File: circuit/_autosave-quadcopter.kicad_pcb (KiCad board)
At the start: 4 copper layers, 37.7 x 37.7 mm, 117 parts, among them J1 Conn_01x01_Female, J10 Conn_01x01_Female, J12 Conn_01x01_Female, J13 Conn_01x01_Female, J15 Conn_01x01_Female, J16 Conn_01x01_Female, J17 Conn_01x01_Female, J18 USB_C_Receptacle_USB2.0, J19 Conn_01x08_Male, J2 Conn_01x01_Female, J21 Conn_01x01_Female, J22 Conn_01x01_Female, J23 Conn_01x01_Female, J24 Conn_01x01_Female, J25 Conn_01x01_Female, J26 Conn_01x01_Female, J28 Conn_01x01_Female, J29 Conn_01x01_Female, J30 Conn_01x01_Female, J31 Conn_01x01_Female, J32 Conn_01x01_Female, J33 Conn_01x01_Female, J34 Conn_01x01_Female, J36 Conn_01x01_Female, J37 Conn_01x01_Female, J38 Conn_01x01_Female, J39 Conn_01x01_Female, J40 Conn_01x01_Female, J41 Conn_01x01_Female, J42 Conn_01x01_Female, J43 Conn_01x01_Female, J44 Conn_01x01_Female, J45 Conn_01x01_Female, J46 Conn_01x01_Female, J47 Conn_01x01_Female, J48 Conn_01x01_Female, J49 Conn_01x01_Female, J5 Conn_Coaxial, J50 Conn_01x01_Female, J6 Conn_01x06_Male, J7 Conn_01x01_Female, J8 Conn_01x01_Female, J9 Conn_01x01_Female, SW1 SW_DIP_x01, U1 STM32G431CBU6, U2 ICM-42605, U3 DPS310, U4 3V3, U5 5V, U6 AT7456E, U7 W25Q128JVS, U8 SX1281, Y1 16M, Y2 27M

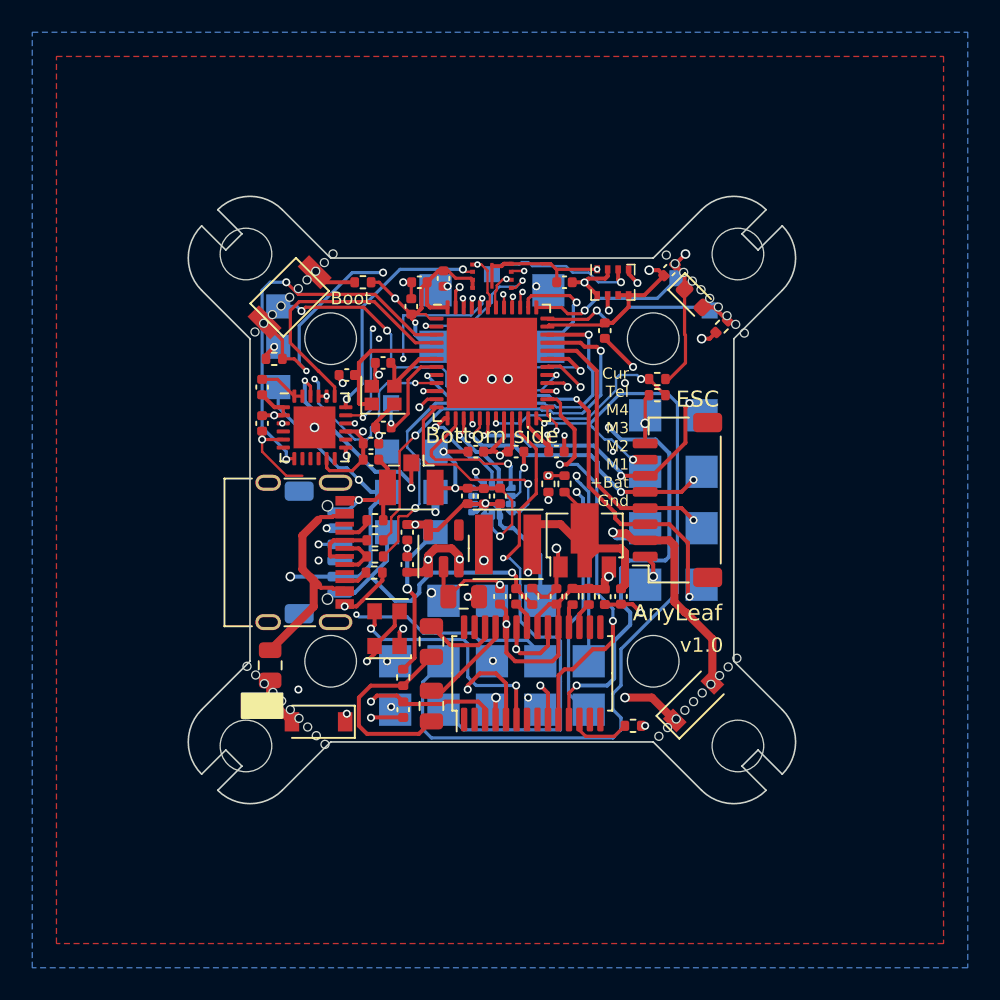
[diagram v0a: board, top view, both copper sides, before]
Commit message: Added buzzer supporting circuitry. Minor code changes
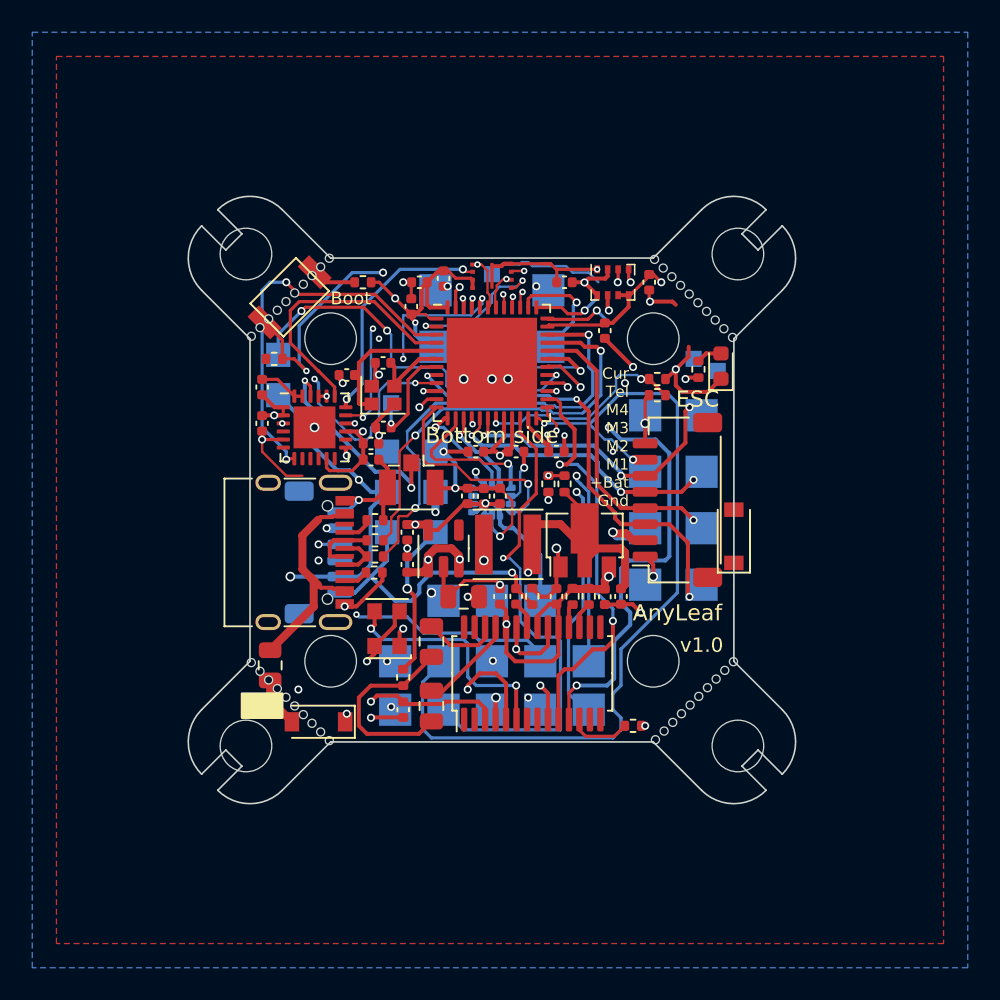
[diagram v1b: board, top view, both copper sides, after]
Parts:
- removed J36: Conn_01x01_Female, TestPoint:TestPoint_Pad_1.5x1.5mm
- moved D2 10.6 mm to (152.0, 89.8), turned to 90 degrees
- moved J2 5.10 mm to (149.5, 78.8)
- moved D3 4.53 mm to (151.2, 79.2), turned to 90 degrees
- moved J1 3.78 mm to (151.0, 79.5)
- moved R12 3.02 mm to (149.8, 79.4), turned to -90 degrees
- moved J31 3.00 mm to (123.8, 78.5)
- moved J37 3.00 mm to (123.8, 81.0)
- moved C2 1.46 mm to (146.8, 74.0), turned to 90 degrees
- moved H12 1.00 mm to (149.5, 75.0)
- moved H9 0.50 mm to (124.5, 100.0)
- moved H11 0.08 mm to (149.6, 99.9)
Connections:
- net /BUZZER+ renamed /BUZZER-
- J37 pad 1: GND -> +5V
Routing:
- net /BAT_IN: track 36.0 -> 20.9 mm, vias 3 -> 2
- net /SWDIO: track 11.2 -> 4.46 mm
- net /SWCLK: track 9.82 -> 4.30 mm
- net /BUZZER-: track 22.1 -> 23.9 mm
- net /SDA2: track 20.3 -> 18.9 mm
- net GND: track 146.6 -> 145.8 mm, vias 37 -> 36
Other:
- board text added: "Bz-"
- board text removed: "Bz"

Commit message: Several changes to PCB to improve voltage capacity of caps, reduce diode size, and accomodate mousebites
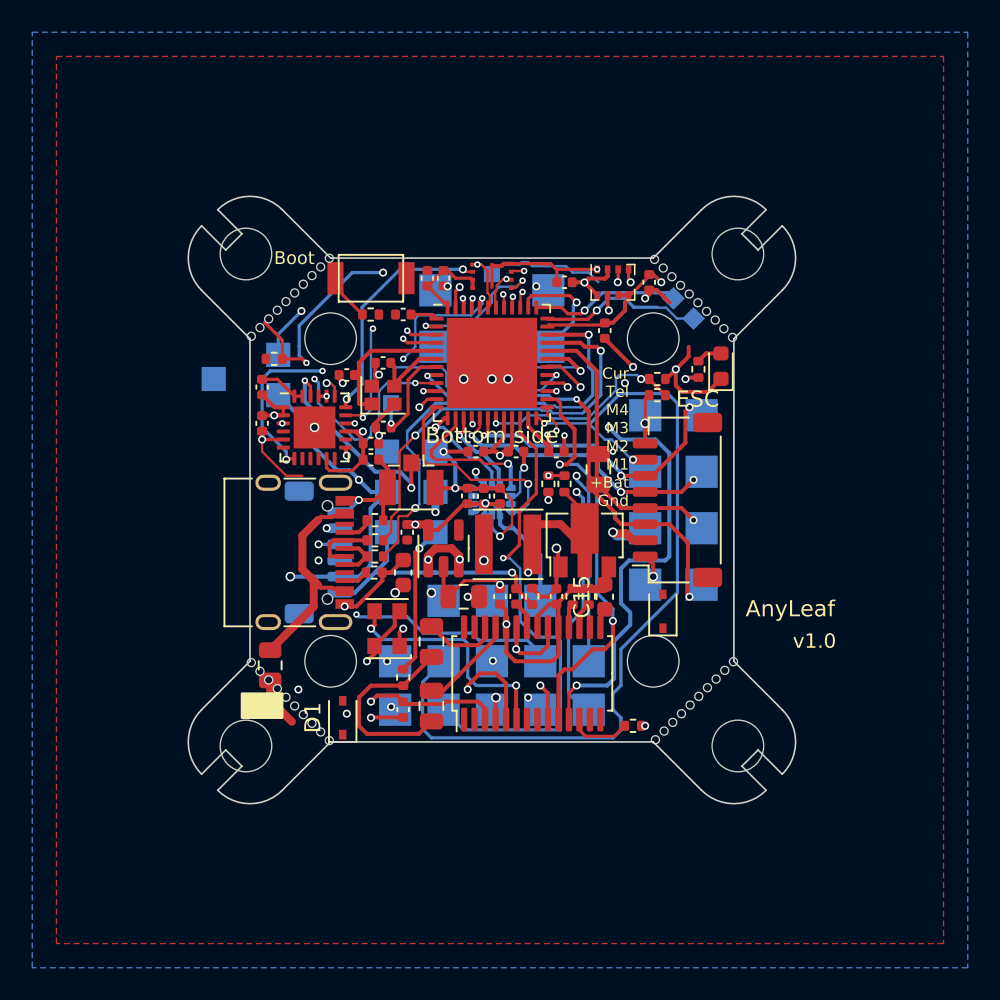
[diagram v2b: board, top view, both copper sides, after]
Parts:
- added J3: Conn_01x01_Female, TestPoint:TestPoint_Pad_1.5x1.5mm, B.Cu at (119.8, 80.0)
- C14: value 10u -> 10uF 50V; footprint Capacitor_SMD:C_0402_1005Metric -> Capacitor_SMD:C_0805_2012Metric
- C15: value 10u -> 10uF 10V; footprint Capacitor_SMD:C_0402_1005Metric -> Capacitor_SMD:C_0603_1608Metric
- C27: value 47u -> 22u 35v
- C7: value 1u -> 1u 50V; footprint Capacitor_SMD:C_0402_1005Metric -> Capacitor_SMD:C_0603_1608Metric
- D1, D2: value MBR0530 -> 40v 1A B5819WS; footprint Diode_SMD:D_SOD-123 -> Diode_SMD:D_SOD-323
- moved C14 8.00 mm to (143.6, 85.6), turned to -90 degrees
- moved D2 6.40 mm to (147.6, 94.4)
- moved SW1 5.18 mm to (129.5, 73.8), turned to 180 degrees
- moved J2 3.95 mm to (148.2, 75.0), turned to 45 degrees
- moved J1 3.58 mm to (149.5, 76.2), turned to 45 degrees
- moved R6 2.06 mm to (129.5, 76.0)
- moved D1 1.52 mm to (127.8, 101.0), turned to 90 degrees
- moved C16 0.71 mm to (131.5, 76.0), turned to 0 degrees
- moved C11 0.56 mm to (133.0, 73.8), turned to -90 degrees
- moved C7 0.56 mm to (131.5, 92.0)
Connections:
- net /BUZZER- renamed /BUZZER_PWM
- U1 pad 9: /ELRS_RST -> /ELRS_DIO
- U8 pad 3: /ELRS_RST -> unconnected-(U8-Pad3)
- U8 pad 8: unconnected-(U8-Pad8) -> /ELRS_DIO
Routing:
- net unconnected-(U8-Pad3): track 0.00 -> 16.2 mm, vias 0 -> 3
- net /ELRS_RST: track 16.2 -> 0.00 mm, vias 3 -> 0
- net +3V3: track 106.0 -> 93.8 mm, vias 12 -> 10
- net /BUZZER_PWM: track 23.9 -> 15.4 mm, vias 3 -> 2
- net /CS_ELRS: track 17.6 -> 9.22 mm, vias 0 -> 2
- net /SWDIO: track 4.46 -> 10.2 mm
- net /ELRS_BUSY: track 24.0 -> 18.3 mm, vias 2 -> 3
- net +BATT: track 39.5 -> 34.2 mm
- net /SWCLK: track 4.30 -> 9.35 mm
- net GND: track 145.8 -> 142.1 mm, vias 36 -> 33
- net /VID_IN: track 18.4 -> 16.8 mm
- net +5V: track 50.8 -> 49.2 mm
- net /VID_OUT: track 17.7 -> 17.1 mm
- net /UART1_TX: track 49.1 -> 48.5 mm, vias 4 -> 3

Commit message: More work on PCB, and ELRS code
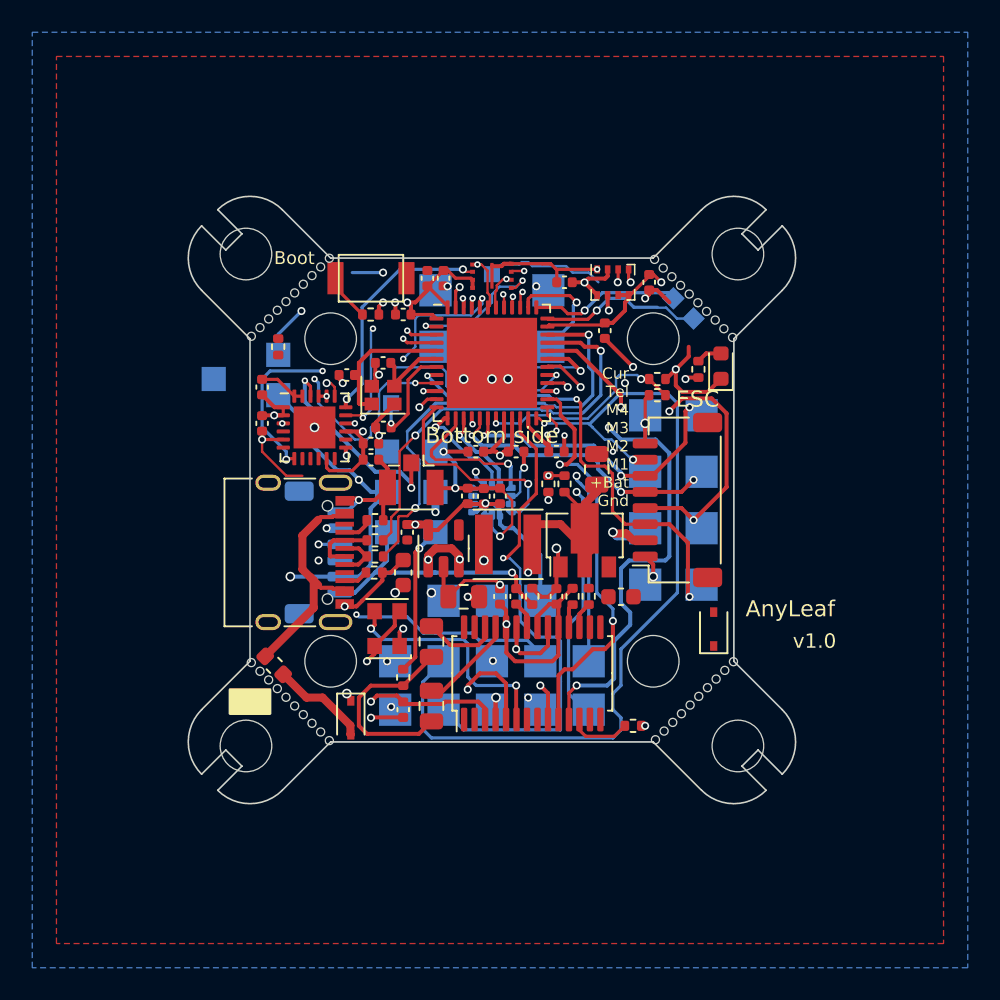
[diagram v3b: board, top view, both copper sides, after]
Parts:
- F1: value 6V, 2.2A -> 6V, 500mA-1A; footprint Fuse:Fuse_0805_2012Metric -> Fuse:Fuse_0603_1608Metric
- moved D2 3.34 mm to (150.8, 95.5)
- moved C15 1.00 mm to (145.0, 93.5), turned to 180 degrees
- moved R1 0.79 mm to (123.8, 78.0), turned to 90 degrees
- moved D1 0.50 mm to (128.2, 101.0), turned to -90 degrees
- moved F1 0.25 mm to (123.5, 97.8), turned to 135 degrees
- moved C14 0.10 mm to (143.5, 85.6)
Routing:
- net GND: track 142.1 -> 156.3 mm
- net /BOOT0: track 20.2 -> 8.72 mm, vias 3 -> 2
- net /UART1_TX: track 48.5 -> 39.7 mm
- net /M2: track 17.5 -> 24.6 mm, vias 1 -> 3
- net +BATT: track 34.2 -> 39.2 mm
- net +3V3: track 93.8 -> 97.4 mm, vias 10 -> 12
- net Net-(D1-Pad2): track 3.12 -> 6.07 mm
- net /M1: track 27.3 -> 27.9 mm
- net Net-(J18-PadA4): track 14.5 -> 15.0 mm

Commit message: More work on translating rx, and PCB
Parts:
- moved J31 6.02 mm to (127.8, 74.0)
- moved J3 4.47 mm to (123.8, 78.0)
- moved D2 1.41 mm to (149.8, 94.5), turned to 180 degrees
- moved R6 0.72 mm to (130.0, 75.5), turned to 90 degrees
- turned C15 to 0 degrees
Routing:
- net GND: track 156.3 -> 183.3 mm, vias 33 -> 38
- net +3V3: track 97.4 -> 115.0 mm
- net /ELRS_DIO: track 0.00 -> 17.5 mm, vias 0 -> 2
- net unconnected-(U8-Pad3): track 16.2 -> 0.00 mm, vias 3 -> 0
- net /BAT_IN: track 20.9 -> 15.1 mm
- net Net-(C15-Pad2): track 0.31 -> 5.82 mm
- net /BUZZER_PWM: track 15.4 -> 19.9 mm, vias 2 -> 3
- net +5V: track 49.1 -> 52.1 mm, vias 11 -> 14
- net Net-(R6-Pad1): track 2.94 -> 3.98 mm
- net /MISO_3: track 18.6 -> 17.7 mm
- net /M1: track 27.9 -> 27.1 mm
- net /BOOT0: track 8.72 -> 9.13 mm, vias 2 -> 3
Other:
- board text added: "UART"
- board text removed: "UART (misc)"

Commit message: More work on tweaking PCB layout
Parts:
- removed F1: 6V, 500mA-1A, Fuse:Fuse_0603_1608Metric
- U5: value 5V -> 5V out, 30V max
- moved C6 4.42 mm to (131.2, 82.8), turned to 180 degrees
- moved D1 1.77 mm to (130.0, 100.8)
- moved C18 1.23 mm to (131.2, 83.8)
- moved R16 0.50 mm to (147.2, 81.5)
- moved R18 0.50 mm to (147.2, 80.5)
- moved R12 0.35 mm to (149.8, 79.8)
- moved C10 0.25 mm to (143.8, 77.0)
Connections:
- D1 pad 2: Net-(D1-Pad2) -> Net-(J18-PadA4)
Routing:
- net Net-(C24-Pad1): track 12.3 -> 2.51 mm
- net /BOOT0: track 9.13 -> 17.7 mm, vias 3 -> 4
- net GND: track 183.3 -> 174.8 mm
- net Net-(J18-PadA4): track 15.0 -> 22.0 mm
- net Net-(D1-Pad2): track 6.07 -> 0.00 mm
- net +3V3: track 115.0 -> 118.4 mm
- net /UART3_RX: track 53.1 -> 55.6 mm
- net Net-(C6-Pad2): track 8.44 -> 10.2 mm
- net /SDA2: track 18.9 -> 20.1 mm
- net /NRST: track 6.65 -> 7.71 mm
- net /LOS: track 3.90 -> 4.80 mm
- net +5V: track 52.1 -> 51.5 mm, vias 14 -> 13
- net /M2: track 24.6 -> 25.2 mm
- net /CURRENT: track 3.10 -> 2.60 mm

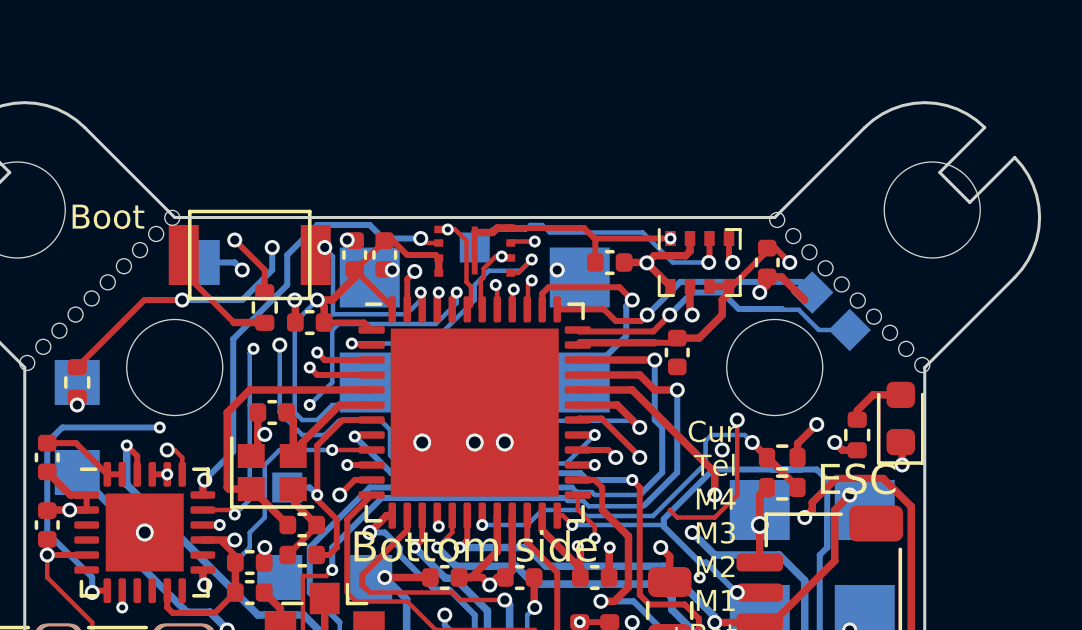
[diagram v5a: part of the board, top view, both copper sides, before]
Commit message: PCB tweaks to clear space around moutning holes. More work translating ELRS.
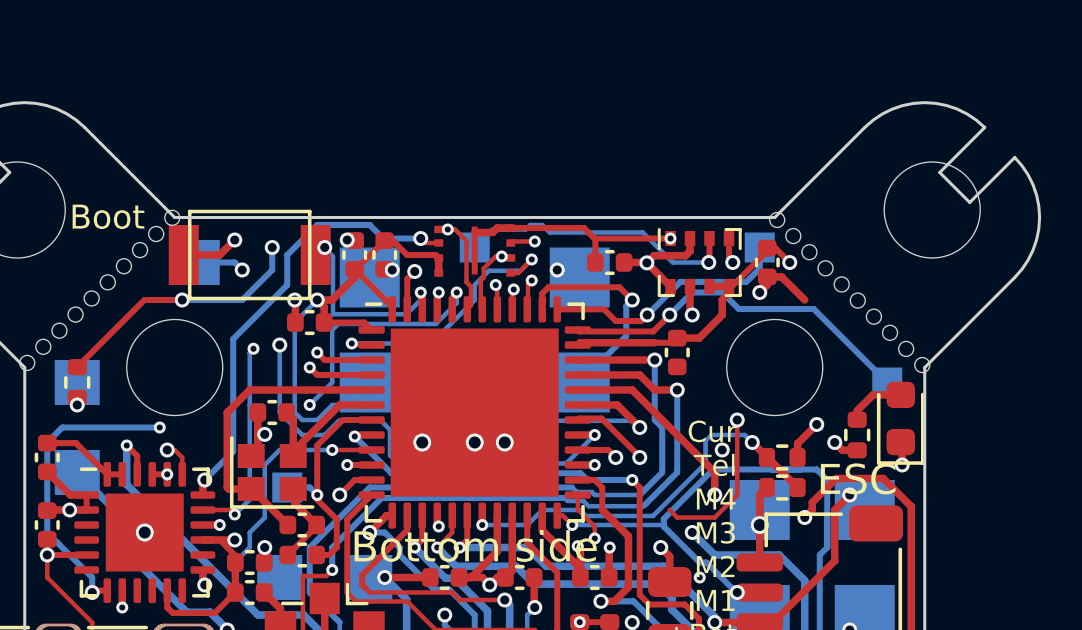
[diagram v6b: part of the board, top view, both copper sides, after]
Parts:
- removed R6: 510, Resistor_SMD:R_0402_1005Metric
- moved J2 2.30 mm to (146.5, 73.5), turned to 0 degrees
- moved J1 2.15 mm to (150.8, 78.0), turned to 0 degrees
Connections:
- SW1 pad 2: Net-(R6-Pad1) -> +3V3
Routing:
- net Net-(R6-Pad1): track 3.98 -> 0.00 mm
- net /SWDIO: track 10.2 -> 12.2 mm
- net /SWCLK: track 9.35 -> 8.34 mm
